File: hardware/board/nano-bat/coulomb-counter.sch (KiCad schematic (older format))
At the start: 8 parts

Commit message: Adding WIP before reverting
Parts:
- removed C? (x3): 4.7u, symbol Device:C
- removed R? (x3): 10k, symbol Device:R_US
- removed U?: LTC4150CMS-PBF, MSOP-10_MS, symbol nano-bat:LTC4150CMS-PBF
- added C? (x2): 1.u, symbol Device:C
- added C? (x2): 4.7u, symbol Device:C
- added JP?: Jumper_3_Bridged12, symbol Jumper:Jumper_3_Bridged12
- added R?: 1.11, symbol Device:R_US
- added R?: 101m, symbol Device:R_US
- added R? (x2): 2.2k, symbol Device:R_US
- added U?: LTC2942, symbol nano-bat:LTC2942
- R?: value R_US -> 10
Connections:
- net labels added: +2V8, SCL, SDA, ~AL~CC
- net labels removed: +3.3V, GNDPWR, POL, ~INT, ~SHDN
- wire segments 37 -> 40

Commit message: Adding first-pass revisions and annotations, part selection
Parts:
- removed C? (x2): 1.u, symbol Device:C
- removed C?: 4.7u, symbol Device:C
- removed R?: 2.2k, symbol Device:R_US
- added C401: 0.1u, Capacitor_SMD:C_0603_1608Metric, symbol Device:C
- added R401: 2.2k, Resistor_SMD:R_0603_1608Metric, symbol Device:R_US
- added R403: 10k, Resistor_SMD:R_0603_1608Metric, symbol Device:R_US
- C402: renamed from C?; value 4.7u -> 1u; footprint (none) -> Capacitor_SMD:C_0603_1608Metric; Part (none) -> 1276-1182-1-ND
- JP401: renamed from JP?; footprint (none) -> Connector_PinHeader_2.54mm:PinHeader_1x03_P2.54mm_Vertical_SMD_Pin1Left; Part (none) -> SAM8981-ND
- R402: renamed from R?; footprint (none) -> Resistor_SMD:R_0603_1608Metric; Part (none) -> P2.2KGCT-ND
- R404: renamed from R?; value 101m -> 100m; footprint (none) -> Resistor_SMD:R_0603_1608Metric; Part (none) -> 273-KDV06DR100ETCT-ND
- R405: renamed from R?; value 1.11 -> 1.1; footprint (none) -> Resistor_SMD:R_1206_3216Metric; Part (none) -> RNCP1206FTD1R00CT-ND
- R406: renamed from R?; footprint (none) -> footprints:SM6227; Part (none) -> SM6227FT10R0
- U401: renamed from U?; footprint (none) -> Package_DFN_QFN:DFN-6-1EP_3x2mm_P0.5mm_EP1.65x1.35mm; Part (none) -> LTC2942CDCB#TRMPBFCT-ND
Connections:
- net +2V8: now also R401.1, R403.2
- net GND: now also C401.1
- net SDA: now also R401.2
- net Vbatt_source: now also C401.2
- net ~AL~CC: now also R403.1
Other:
- note removed: "Note that VDD is sourced off the simulated battery,\nsince it is assumed that the battery has infinite supply.\nThis results in a parasitic load whenever a real battery is\nused."
- moved on the sheet: C402, JP401, R402, R404, R405, R406

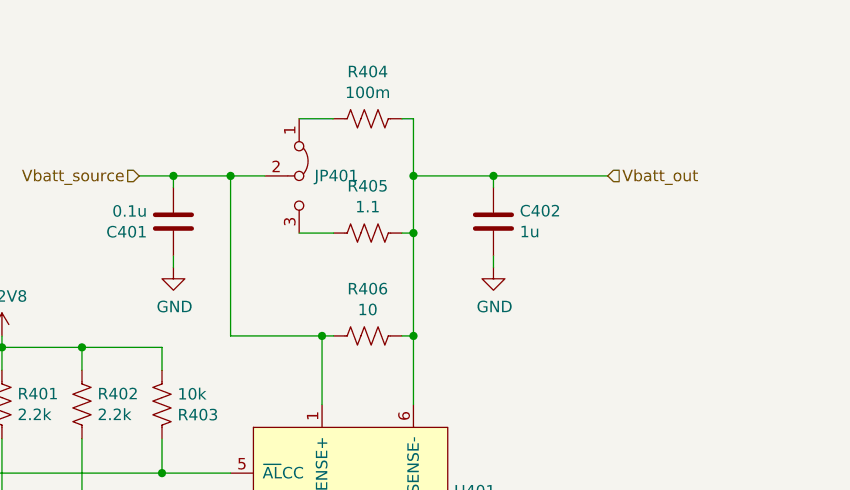
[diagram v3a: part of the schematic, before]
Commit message: Adding docs to schematic
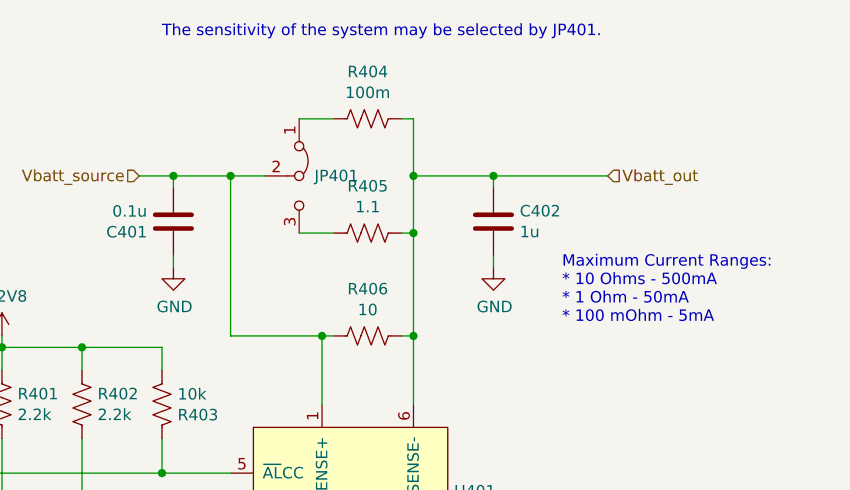
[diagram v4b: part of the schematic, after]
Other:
- note added: "Maximum Current Ranges:\n* 10 Ohms - 500mA\n* 1 Ohm - 50mA\n* 100 mOhm - 5mA"
- note added: "The sensitivity of the system may be selected by JP401."
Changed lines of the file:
@@
 	-1   0    0    1
 $EndComp
+Text Notes 4950 1650 0    50   ~ 0
+The sensitivity of the system may be selected by JP401.
+Text Notes 6700 2900 0    50   ~ 0
+Maximum Current Ranges:\n* 10 Ohms - 500mA\n* 1 Ohm - 50mA\n* 100 mOhm - 5mA
 $EndSCHEMATC

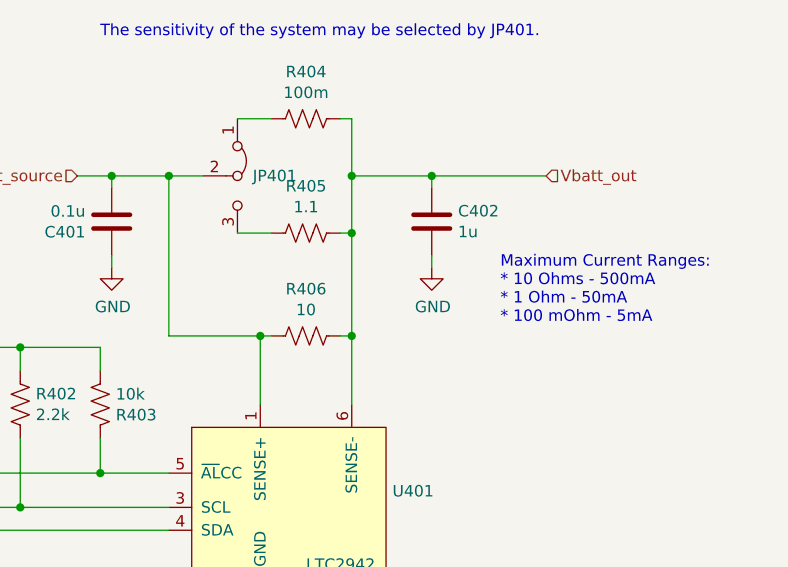
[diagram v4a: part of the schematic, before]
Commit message: Adding test points, initial board outline
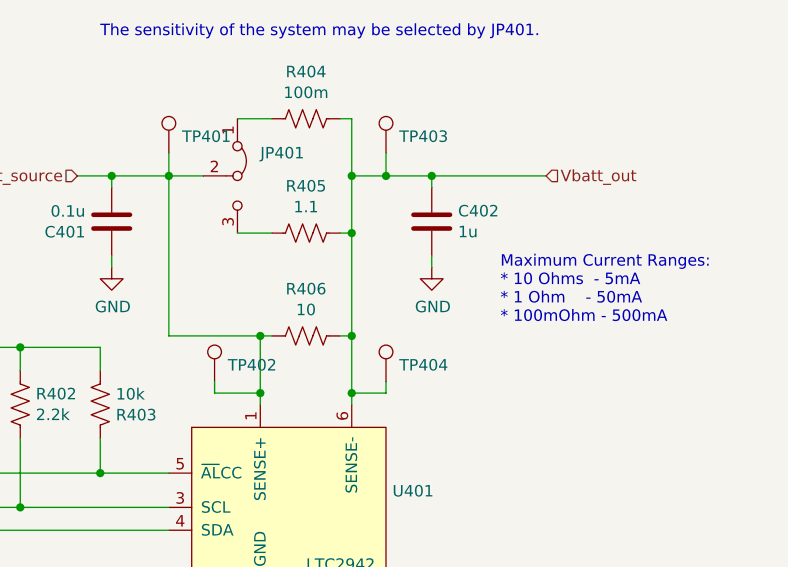
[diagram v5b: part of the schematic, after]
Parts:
- added TP401, TP402, TP403, TP404: TestPoint, symbol Connector:TestPoint
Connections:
- net Vbatt_out: now also TP403.1, TP404.1
- net Vbatt_source: now also TP401.1, TP402.1
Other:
- note added: "Maximum Current Ranges:\n* 10 Ohms - 5mA\n* 1 Ohm - 50mA\n* 100mOhm - 500mA"
- note removed: "Maximum Current Ranges:\n* 10 Ohms - 500mA\n* 1 Ohm - 50mA\n* 100 mOhm - 5mA"
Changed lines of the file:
@@
 Comment4 ""
 $EndDescr
-$Comp
-L Device:R_US R406
-U 1 1 5DDBBCC5
-P 5850 2950
-F 0 "R406" V 5645 2950 50  0000 C CNN
-F 1 "10" V 5736 2950 50  0000 C CNN
-F 2 "footprints:SM6227" V 5890 2940 50  0001 C CNN
-F 3 "~" H 5850 2950 50  0001 C CNN
-F 4 "SM6227FT10R0" V 5850 2950 50  0001 C CNN "Part"
-	1    5850 2950
-	0    1    1    0
-$EndComp
 Text HLabel 4850 2250 0    50   Input ~ 0
 Vbatt_source
@@
 Connection ~ 6050 2950
 Wire Wire Line
-	6050 2250 6400 2250
-$Comp
-L Device:R_US R405
-U 1 1 5DDB5613
-P 5850 2500
-F 0 "R405" V 5645 2500 50  0000 C CNN
-F 1 "1.1" V 5736 2500 50  0000 C CNN
-F 2 "Resistor_SMD:R_1206_3216Metric" V 5890 2490 50  0001 C CNN
-F 3 "~" H 5850 2500 50  0001 C CNN
-F 4 "RNCP1206FTD1R00CT-ND" V 5850 2500 50  0001 C CNN "Part"
-	1    5850 2500
-	0    1    1    0
-$EndComp
+	6050 2250 6200 2250
 $Comp
 L nano-bat:LTC2942 U401
@@
 Text HLabel 4050 3800 0    50   Input ~ 0
 SDA
-$Comp
-L Device:R_US R404
-U 1 1 5DDBF8CD
-P 5850 2000
-F 0 "R404" V 5645 2000 50  0000 C CNN
-F 1 "100m" V 5736 2000 50  0000 C CNN
-F 2 "Resistor_SMD:R_0603_1608Metric" V 5890 1990 50  0001 C CNN
-F 3 "~" H 5850 2000 50  0001 C CNN
-F 4 "273-KDV06DR100ETCT-ND" V 5850 2000 50  0001 C CNN "Part"
-	1    5850 2000
-	0    1    1    0
-$EndComp
 Wire Wire Line
 	5700 2000 5550 2000
@@
 U 1 1 5DDC0EDA
 P 5550 2250
-F 0 "JP401" V 5550 2317 50  0000 L CNN
+F 0 "JP401" V 5450 2350 50  0000 L CNN
 F 1 "Jumper_3_Bridged12" V 5595 2317 50  0001 L CNN
 F 2 "Connector_PinHeader_2.54mm:PinHeader_1x03_P2.54mm_Vertical_SMD_Pin1Left" H 5550 2250 50  0001 C CNN
@@
 Connection ~ 4250 3800
 Wire Wire Line
-	5250 2950 5650 2950
-Wire Wire Line
 	5250 2950 5250 2250
 Connection ~ 5250 2250
@@
 $EndBitmap
 Wire Wire Line
-	5650 2950 5650 3250
-Wire Wire Line
-	6050 2950 6050 3250
-Wire Wire Line
 	4600 3000 4950 3000
 Wire Wire Line
@@
 Text Notes 4950 1650 0    50   ~ 0
 The sensitivity of the system may be selected by JP401.
+Wire Wire Line
+	6050 2950 6050 3200
+Wire Wire Line
+	5650 2950 5650 3200
+Wire Wire Line
+	5250 2950 5650 2950
+$Comp
+L Device:R_US R406
+U 1 1 5DDBBCC5
+P 5850 2950
+F 0 "R406" V 5645 2950 50  0000 C CNN
+F 1 "10" V 5736 2950 50  0000 C CNN
+F 2 "footprints:SM6227" V 5890 2940 50  0001 C CNN
+F 3 "~" H 5850 2950 50  0001 C CNN
+F 4 "SM6227FT10R0" V 5850 2950 50  0001 C CNN "Part"
+	1    5850 2950
+	0    1    1    0
+$EndComp
 Text Notes 6700 2900 0    50   ~ 0
-Maximum Current Ranges:\n* 10 Ohms - 500mA\n* 1 Ohm - 50mA\n* 100 mOhm - 5mA
+Maximum Current Ranges:\n* 10 Ohms  - 5mA\n* 1 Ohm    - 50mA\n* 100mOhm - 500mA
+$Comp
+L Device:R_US R405
+U 1 1 5DDB5613
+P 5850 2500
+F 0 "R405" V 5645 2500 50  0000 C CNN
+F 1 "1.1" V 5736 2500 50  0000 C CNN
+F 2 "Resistor_SMD:R_1206_3216Metric" V 5890 2490 50  0001 C CNN
+F 3 "~" H 5850 2500 50  0001 C CNN
+F 4 "RNCP1206FTD1R00CT-ND" V 5850 2500 50  0001 C CNN "Part"
+	1    5850 2500
+	0    1    1    0
+$EndComp
+$Comp
+L Device:R_US R404
+U 1 1 5DDBF8CD
+P 5850 2000
+F 0 "R404" V 5645 2000 50  0000 C CNN
+F 1 "100m" V 5736 2000 50  0000 C CNN
+F 2 "Resistor_SMD:R_0603_1608Metric" V 5890 1990 50  0001 C CNN
+F 3 "~" H 5850 2000 50  0001 C CNN
+F 4 "273-KDV06DR100ETCT-ND" V 5850 2000 50  0001 C CNN "Part"
+	1    5850 2000
+	0    1    1    0
+$EndComp
+$Comp
+L Connector:TestPoint TP404
+U 1 1 5E1E5CF9
+P 6200 3150
+F 0 "TP404" H 6258 3222 50  0000 L CNN
+F 1 "TestPoint" H 6258 3177 50  0001 L CNN
+F 2 "" H 6400 3150 50  0001 C CNN
+F 3 "~" H 6400 3150 50  0001 C CNN
+	1    6200 3150
+	1    0    0    -1
+$EndComp
+$Comp
+L Connector:TestPoint TP402
+U 1 1 5E1E6532
+P 5450 3150
+F 0 "TP402" H 5508 3222 50  0000 L CNN
+F 1 "TestPoint" H 5508 3177 50  0001 L CNN
+F 2 "" H 5650 3150 50  0001 C CNN
+F 3 "~" H 5650 3150 50  0001 C CNN
+	1    5450 3150
+	1    0    0    -1
+$EndComp
+Wire Wire Line
+	5450 3150 5450 3200
+Wire Wire Line
+	5450 3200 5650 3200
+Connection ~ 5650 3200
+Wire Wire Line
+	5650 3200 5650 3250
+Wire Wire Line
+	6200 3150 6200 3200
+Wire Wire Line
+	6200 3200 6050 3200
+Connection ~ 6050 3200
+Wire Wire Line
+	6050 3200 6050 3250
+$Comp
+L Connector:TestPoint TP401
+U 1 1 5E1E78CD
+P 5250 2150
+F 0 "TP401" H 5308 2222 50  0000 L CNN
+F 1 "TestPoint" H 5308 2177 50  0001 L CNN
+F 2 "" H 5450 2150 50  0001 C CNN
+F 3 "~" H 5450 2150 50  0001 C CNN
+	1    5250 2150
+	1    0    0    -1
+$EndComp
+Wire Wire Line
+	5250 2150 5250 2250
+$Comp
+L Connector:TestPoint TP403
+U 1 1 5E1E85DA
+P 6200 2150
+F 0 "TP403" H 6258 2222 50  0000 L CNN
+F 1 "TestPoint" H 6258 2177 50  0001 L CNN
+F 2 "" H 6400 2150 50  0001 C CNN
+F 3 "~" H 6400 2150 50  0001 C CNN
+	1    6200 2150
+	1    0    0    -1
+$EndComp
+Wire Wire Line
+	6200 2150 6200 2250
+Connection ~ 6200 2250
+Wire Wire Line
+	6200 2250 6400 2250
 $EndSCHEMATC

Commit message: Updating test points, adding 3d models
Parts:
- TP401, TP402, TP403, TP404: footprint (none) -> TestPoint:TestPoint_Pad_2.0x2.0mm; Part (none) -> A106144CT-ND
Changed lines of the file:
@@
 F 0 "TP404" H 6258 3222 50  0000 L CNN
 F 1 "TestPoint" H 6258 3177 50  0001 L CNN
-F 2 "" H 6400 3150 50  0001 C CNN
+F 2 "TestPoint:TestPoint_Pad_2.0x2.0mm" H 6400 3150 50  0001 C CNN
 F 3 "~" H 6400 3150 50  0001 C CNN
+F 4 "A106144CT-ND" H 6200 3150 50  0001 C CNN "Part"
 	1    6200 3150
 	1    0    0    -1
@@
 F 0 "TP402" H 5508 3222 50  0000 L CNN
 F 1 "TestPoint" H 5508 3177 50  0001 L CNN
-F 2 "" H 5650 3150 50  0001 C CNN
+F 2 "TestPoint:TestPoint_Pad_2.0x2.0mm" H 5650 3150 50  0001 C CNN
 F 3 "~" H 5650 3150 50  0001 C CNN
+F 4 "A106144CT-ND" H 5450 3150 50  0001 C CNN "Part"
 	1    5450 3150
 	1    0    0    -1
@@
 F 0 "TP401" H 5308 2222 50  0000 L CNN
 F 1 "TestPoint" H 5308 2177 50  0001 L CNN
-F 2 "" H 5450 2150 50  0001 C CNN
+F 2 "TestPoint:TestPoint_Pad_2.0x2.0mm" H 5450 2150 50  0001 C CNN
 F 3 "~" H 5450 2150 50  0001 C CNN
+F 4 "A106144CT-ND" H 5250 2150 50  0001 C CNN "Part"
 	1    5250 2150
 	1    0    0    -1
@@
 F 0 "TP403" H 6258 2222 50  0000 L CNN
 F 1 "TestPoint" H 6258 2177 50  0001 L CNN
-F 2 "" H 6400 2150 50  0001 C CNN
+F 2 "TestPoint:TestPoint_Pad_2.0x2.0mm" H 6400 2150 50  0001 C CNN
 F 3 "~" H 6400 2150 50  0001 C CNN
+F 4 "A106144CT-ND" H 6200 2150 50  0001 C CNN "Part"
 	1    6200 2150
 	1    0    0    -1
